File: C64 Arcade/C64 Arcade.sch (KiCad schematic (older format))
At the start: 59 parts, among them J1 Port_1, J10 P2_FIRE3, J11 P1_FIRE1, J12 P1_FIRE2, J13 P1_FIRE3, J14 EXT_PWR, J15 DIR_LEFT, J2 Port_2, J3 DIR_RIGHT, J4 UP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

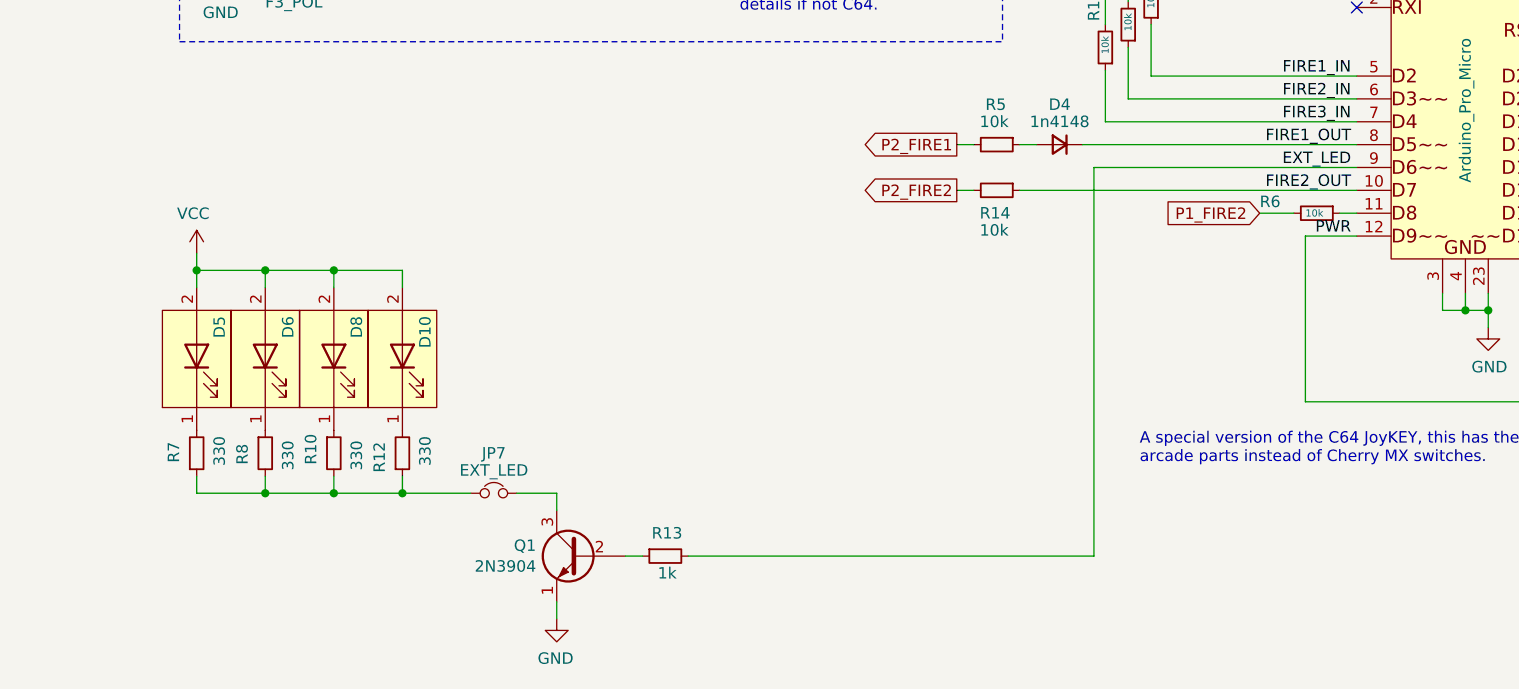
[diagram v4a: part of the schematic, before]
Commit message: New arcade layout
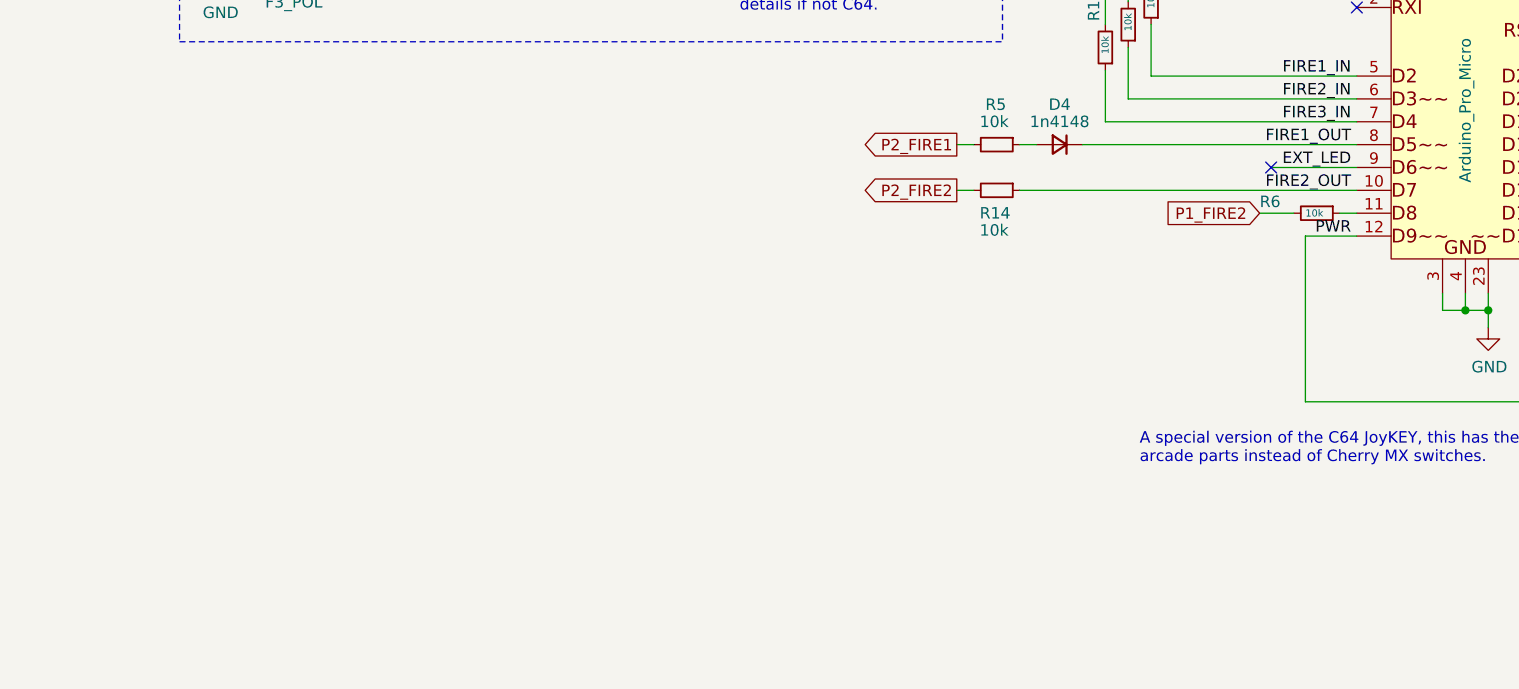
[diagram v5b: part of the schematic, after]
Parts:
- removed D10, D5, D6, D8: LED_Plugin, Connector_JST:JST_XH_B2B-XH-A_1x02_P2.50mm_Vertical, symbol arcade:LED_Plugin
- removed JP7: EXT_LED, Connector_PinHeader_2.54mm:PinHeader_1x02_P2.54mm_Horizontal, symbol Device:Jumper_NC_Small
- removed Q1: 2N3904, 2n3904:2N3904_TO-92_Horizontal_FlatSideDown, symbol Transistor_BJT:2N3904
- removed R10, R12, R7, R8: 330, Resistor_THT:R_Axial_DIN0207_L6.3mm_D2.5mm_P10.16mm_Horizontal, symbol Device:R_Small
- removed R13: 1k, Resistor_THT:R_Axial_DIN0207_L6.3mm_D2.5mm_P10.16mm_Horizontal, symbol Device:R_Small
- D3: footprint Diodes_THT:D_DO-41_SOD81_P10.16mm_Horizontal -> Diode_THT:D_DO-41_SOD81_P10.16mm_Horizontal
- J15: footprint (none) -> Connector_JST:JST_XH_B5B-XH-A_1x05_P2.50mm_Vertical
- JP1, JP2, JP3: footprint Pin_Headers:Pin_Header_Angled_1x03_Pitch2.54mm -> Connector_PinHeader_2.54mm:PinHeader_1x03_P2.54mm_Horizontal
- SW8: footprint Buttons_Switches_THT:SW_PUSH_6mm -> Button_Switch_THT:SW_PUSH_6mm
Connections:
- no-connect marks 8 -> 9
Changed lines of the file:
@@
 F 0 "JP3" H 4500 3625 50  0000 C CNN
 F 1 "FIRE3_SEL" H 4625 3700 50  0000 C CNN
-F 2 "Pin_Headers:Pin_Header_Angled_1x03_Pitch2.54mm" H 4400 3775 50  0001 C CNN
+F 2 "Connector_PinHeader_2.54mm:PinHeader_1x03_P2.54mm_Horizontal" H 4400 3775 50  0001 C CNN
 F 3 "~" H 4400 3775 50  0001 C CNN
 	1    4400 3775
@@
 F 0 "JP2" H 3325 4636 50  0000 C CNN
 F 1 "F3_POL" H 3325 4727 50  0000 C CNN
-F 2 "Pin_Headers:Pin_Header_Angled_1x03_Pitch2.54mm" H 3325 4525 50  0001 C CNN
+F 2 "Connector_PinHeader_2.54mm:PinHeader_1x03_P2.54mm_Horizontal" H 3325 4525 50  0001 C CNN
 F 3 "~" H 3325 4525 50  0001 C CNN
 	1    3325 4525
@@
 F 0 "D3" H 9975 1159 50  0000 C CNN
 F 1 "1n4001" H 9975 1250 50  0000 C CNN
-F 2 "Diodes_THT:D_DO-41_SOD81_P10.16mm_Horizontal" H 9975 1375 50  0001 C CNN
+F 2 "Diode_THT:D_DO-41_SOD81_P10.16mm_Horizontal" H 9975 1375 50  0001 C CNN
 F 3 "~" H 9975 1375 50  0001 C CNN
 	1    9975 1375
@@
 	1    0    0    -1
 $EndComp
-$Comp
-L Transistor_BJT:2N3904 Q1
-U 1 1 5FF9EE9A
-P 4575 7150
-F 0 "Q1" H 4765 7196 50  0000 L CNN
-F 1 "2N3904" H 4765 7105 50  0000 L CNN
-F 2 "2n3904:2N3904_TO-92_Horizontal_FlatSideDown" H 4775 7075 50  0001 L CIN
-F 3 "https://www.onsemi.com/pub/Collateral/2N3903-D.PDF" H 4575 7150 50  0001 L CNN
-	1    4575 7150
-	-1   0    0    -1
-$EndComp
-$Comp
-L power:GND #PWR0105
-U 1 1 60445FBA
-P 4475 7425
-F 0 "#PWR0105" H 4475 7175 50  0001 C CNN
-F 1 "GND" H 4480 7252 50  0000 C CNN
-F 2 "" H 4475 7425 50  0001 C CNN
-F 3 "" H 4475 7425 50  0001 C CNN
-	1    4475 7425
-	-1   0    0    -1
-$EndComp
-Wire Wire Line
-	4475 6950 4475 6875
-Wire Wire Line
-	3800 6800 3800 6875
-Wire Wire Line
-	3500 6800 3500 6875
-Wire Wire Line
-	3200 6800 3200 6875
-Wire Wire Line
-	3200 6875 2900 6875
-Wire Wire Line
-	2900 6800 2900 6875
-Wire Wire Line
-	3800 5975 3800 5900
-Wire Wire Line
-	3500 5900 3500 5975
-Wire Wire Line
-	3200 5900 3200 5975
-Wire Wire Line
-	3200 5900 2900 5900
-Wire Wire Line
-	2900 5900 2900 5975
-Connection ~ 2900 5900
-$Comp
-L power:VCC #PWR0106
-U 1 1 60445FBB
-P 2900 5825
-F 0 "#PWR0106" H 2900 5675 50  0001 C CNN
-F 1 "VCC" H 2915 5998 50  0000 C CNN
-F 2 "" H 2900 5825 50  0001 C CNN
-F 3 "" H 2900 5825 50  0001 C CNN
-	1    2900 5825
-	-1   0    0    -1
-$EndComp
-$Comp
-L Device:R_Small R13
-U 1 1 60445FBC
-P 4950 7150
-F 0 "R13" V 4850 7075 50  0000 L CNN
-F 1 "1k" V 5025 7100 50  0000 L CNN
-F 2 "Resistor_THT:R_Axial_DIN0207_L6.3mm_D2.5mm_P10.16mm_Horizontal" H 4950 7150 50  0001 C CNN
-F 3 "~" H 4950 7150 50  0001 C CNN
-	1    4950 7150
-	0    -1   1    0
-$EndComp
-Wire Wire Line
-	4850 7150 4775 7150
 Text GLabel 3400 2575 2    50   Output ~ 0
 FIRE2_POL
@@
 	3325 2575 3325 2675
 Wire Wire Line
-	6825 7150 6825 5450
-$Comp
-L Device:R_Small R7
-U 1 1 60445FBE
-P 2900 6700
-F 0 "R7" V 2800 6650 50  0000 L CNN
-F 1 "330" V 3000 6625 50  0000 L CNN
-F 2 "Resistor_THT:R_Axial_DIN0207_L6.3mm_D2.5mm_P10.16mm_Horizontal" H 2900 6700 50  0001 C CNN
-F 3 "~" H 2900 6700 50  0001 C CNN
-	1    2900 6700
-	1    0    0    1
-$EndComp
-$Comp
-L Device:R_Small R8
-U 1 1 60A50931
-P 3200 6700
-F 0 "R8" V 3100 6650 50  0000 L CNN
-F 1 "330" V 3300 6625 50  0000 L CNN
-F 2 "Resistor_THT:R_Axial_DIN0207_L6.3mm_D2.5mm_P10.16mm_Horizontal" H 3200 6700 50  0001 C CNN
-F 3 "~" H 3200 6700 50  0001 C CNN
-	1    3200 6700
-	1    0    0    -1
-$EndComp
-$Comp
-L Device:R_Small R10
-U 1 1 60152B72
-P 3500 6700
-F 0 "R10" V 3400 6650 50  0000 L CNN
-F 1 "330" V 3600 6625 50  0000 L CNN
-F 2 "Resistor_THT:R_Axial_DIN0207_L6.3mm_D2.5mm_P10.16mm_Horizontal" H 3500 6700 50  0001 C CNN
-F 3 "~" H 3500 6700 50  0001 C CNN
-	1    3500 6700
-	1    0    0    -1
-$EndComp
-$Comp
-L Device:R_Small R12
-U 1 1 60A50933
-P 3800 6700
-F 0 "R12" V 3700 6650 50  0000 L CNN
-F 1 "330" V 3900 6625 50  0000 L CNN
-F 2 "Resistor_THT:R_Axial_DIN0207_L6.3mm_D2.5mm_P10.16mm_Horizontal" H 3800 6700 50  0001 C CNN
-F 3 "~" H 3800 6700 50  0001 C CNN
-	1    3800 6700
-	1    0    0    1
-$EndComp
-Wire Wire Line
-	4475 7425 4475 7350
-Wire Wire Line
 	4400 3625 4400 3550
-$Comp
-L Device:Jumper_NC_Small JP7
-U 1 1 603A8E18
-P 4200 6875
-F 0 "JP7" H 4200 7050 50  0000 C CNN
-F 1 "EXT_LED" H 4200 6975 50  0000 C CNN
-F 2 "Connector_PinHeader_2.54mm:PinHeader_1x02_P2.54mm_Horizontal" H 4200 6875 50  0001 C CNN
-F 3 "~" H 4200 6875 50  0001 C CNN
-	1    4200 6875
-	-1   0    0    -1
-$EndComp
-Wire Wire Line
-	5050 7150 6825 7150
-Wire Wire Line
-	3800 6875 4100 6875
-Wire Wire Line
-	4300 6875 4475 6875
 Text Label 9050 5850 0    50   ~ 0
 SYS
@@
 F 0 "JP1" H 3325 3136 50  0000 C CNN
 F 1 "F2_POL" H 3325 3227 50  0000 C CNN
-F 2 "Pin_Headers:Pin_Header_Angled_1x03_Pitch2.54mm" H 3325 3025 50  0001 C CNN
+F 2 "Connector_PinHeader_2.54mm:PinHeader_1x03_P2.54mm_Horizontal" H 3325 3025 50  0001 C CNN
 F 3 "~" H 3325 3025 50  0001 C CNN
 	1    3325 3025
@@
 Connection ~ 4100 1075
 Connection ~ 4100 2250
-$Comp
-L arcade:LED_Plugin D10
-U 1 1 6013CF33
-P 3800 6275
-F 0 "D10" H 3975 6175 50  0000 R CNN
-F 1 "LED_Plugin" V 3743 6097 50  0001 R CNN
-F 2 "Connector_JST:JST_XH_B2B-XH-A_1x02_P2.50mm_Vertical" H 3800 6275 50  0001 C CNN
-F 3 "~" H 3800 6275 50  0001 C CNN
-	1    3800 6275
-	0    -1   -1   0
-$EndComp
-$Comp
-L arcade:LED_Plugin D8
-U 1 1 6018EAC5
-P 3500 6275
-F 0 "D8" H 3675 6175 50  0000 R CNN
-F 1 "LED_Plugin" V 3443 6097 50  0001 R CNN
-F 2 "Connector_JST:JST_XH_B2B-XH-A_1x02_P2.50mm_Vertical" H 3500 6275 50  0001 C CNN
-F 3 "~" H 3500 6275 50  0001 C CNN
-	1    3500 6275
-	0    -1   -1   0
-$EndComp
-$Comp
-L arcade:LED_Plugin D6
-U 1 1 601A1981
-P 3200 6275
-F 0 "D6" H 3375 6175 50  0000 R CNN
-F 1 "LED_Plugin" V 3143 6097 50  0001 R CNN
-F 2 "Connector_JST:JST_XH_B2B-XH-A_1x02_P2.50mm_Vertical" H 3200 6275 50  0001 C CNN
-F 3 "~" H 3200 6275 50  0001 C CNN
-	1    3200 6275
-	0    -1   -1   0
-$EndComp
-$Comp
-L arcade:LED_Plugin D5
-U 1 1 601AB1C0
-P 2900 6275
-F 0 "D5" H 3075 6175 50  0000 R CNN
-F 1 "LED_Plugin" V 2843 6097 50  0001 R CNN
-F 2 "Connector_JST:JST_XH_B2B-XH-A_1x02_P2.50mm_Vertical" H 2900 6275 50  0001 C CNN
-F 3 "~" H 2900 6275 50  0001 C CNN
-	1    2900 6275
-	0    -1   -1   0
-$EndComp
 $Comp
 L arcade:PWR J14
@@
 	1    0    0    -1
 $EndComp
-Wire Wire Line
-	2900 5825 2900 5900
 Text GLabel 7550 5650 0    50   Input ~ 0
 P1_FIRE2
@@
 	8850 1375 9550 1375
 Wire Wire Line
-	3200 6875 3500 6875
-Connection ~ 3200 6875
-Wire Wire Line
-	3500 6875 3800 6875
-Connection ~ 3500 6875
-Connection ~ 3800 6875
-Wire Wire Line
-	3200 5900 3500 5900
-Connection ~ 3200 5900
-Wire Wire Line
-	3500 5900 3800 5900
-Connection ~ 3500 5900
-Wire Wire Line
 	10200 1375 10275 1375
 Connection ~ 10200 1375
@@
 F 0 "J15" H 830 1025 50  0000 C CNN
 F 1 "DIR_LEFT" H 830 1116 50  0000 C CNN
-F 2 "" H 850 1450 50  0001 C CNN
+F 2 "Connector_JST:JST_XH_B5B-XH-A_1x05_P2.50mm_Vertical" H 850 1450 50  0001 C CNN
 F 3 "~" H 850 1450 50  0001 C CNN
 	1    850  1450
@@
 F 0 "SW8" H 9200 5025 50  0000 C CNN
 F 1 "RESET" H 9200 4775 50  0000 C CNN
-F 2 "Buttons_Switches_THT:SW_PUSH_6mm" H 9200 5050 50  0001 C CNN
+F 2 "Button_Switch_THT:SW_PUSH_6mm" H 9200 5050 50  0001 C CNN
 F 3 "~" H 9200 5050 50  0001 C CNN
 	1    9200 4850
@@
 Wire Wire Line
 	6875 4825 6875 3550
-Wire Wire Line
-	6825 5450 7975 5450
 Text Label 7950 5450 2    50   ~ 0
 EXT_LED
@@
 Wire Wire Line
 	3325 3875 3325 4175
+Wire Wire Line
+	7975 5450 7600 5450
+NoConn ~ 7600 5450
 $EndSCHEMATC

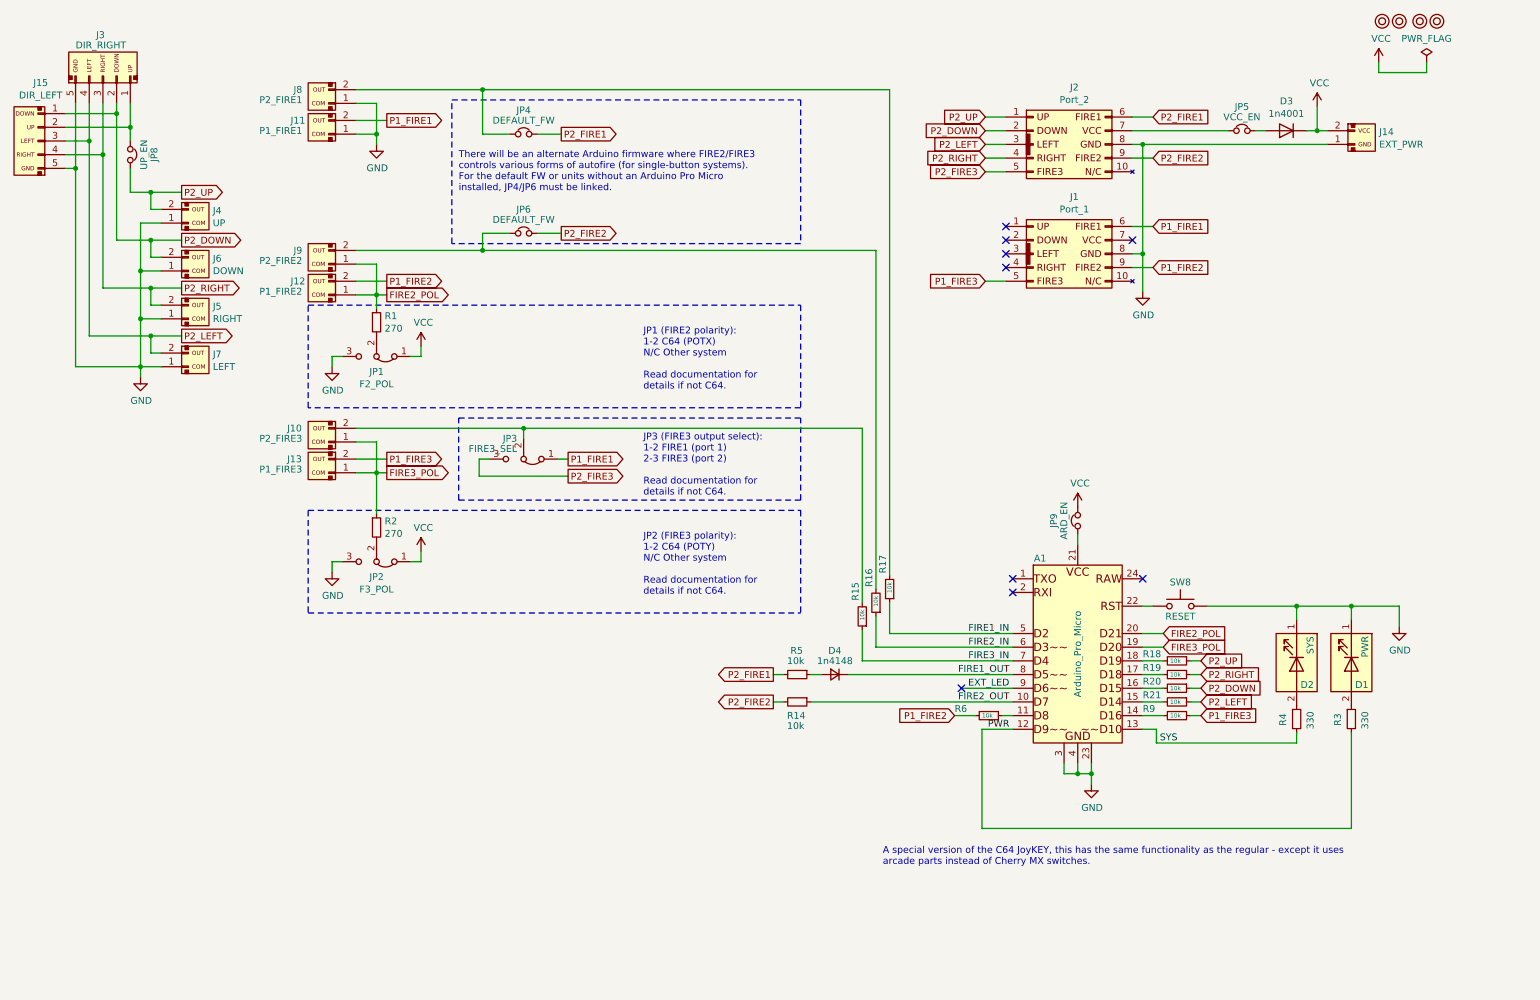
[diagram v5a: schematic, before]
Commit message: Add one more button to arcade board
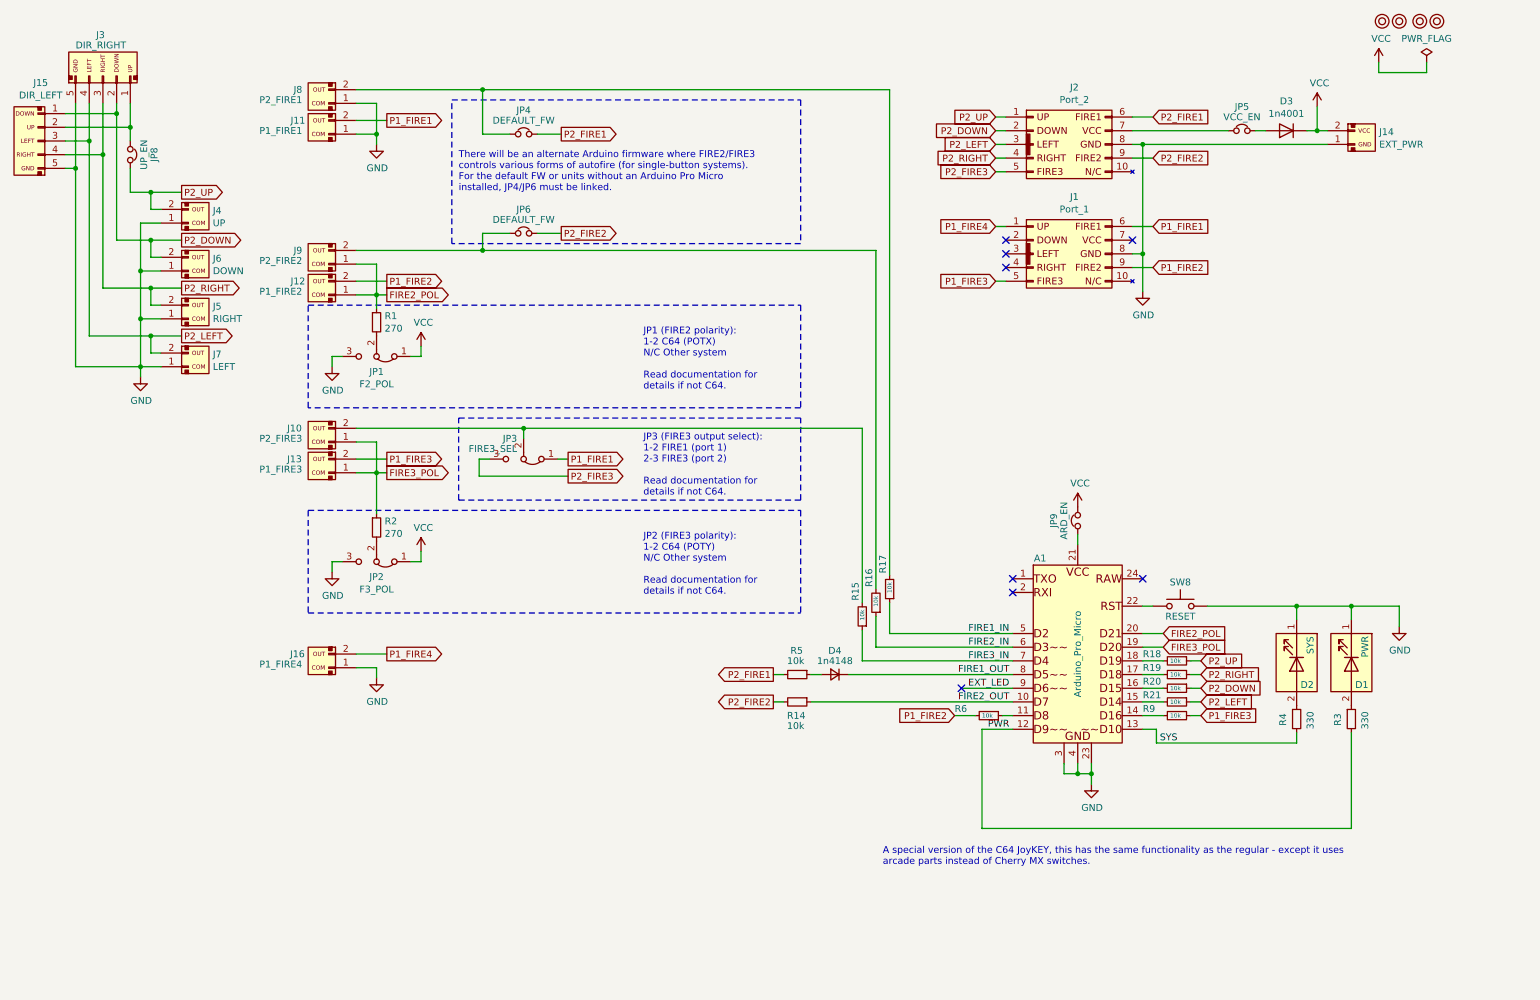
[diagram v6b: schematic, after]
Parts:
- added J16: P1_FIRE4, Connector_JST:JST_XH_B2B-XH-A_1x02_P2.50mm_Vertical, symbol arcade:SWITCH
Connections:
- net GND: now also J16.1 (Pin_1)
- net P1_FIRE4: now reaches J1.1 (Pin_1)
- net P1_FIRE4: now also J16.2 (Pin_2)
- no-connect marks 9 -> 8
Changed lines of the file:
@@
 	1    0    0    -1
 $EndComp
-NoConn ~ 7925 2075
 NoConn ~ 7925 2175
 NoConn ~ 7925 2275
 NoConn ~ 7925 2375
 NoConn ~ 8850 2175
-Text GLabel 7775 1275 0    50   Input ~ 0
+Text GLabel 7850 1275 0    50   Input ~ 0
 P2_UP
-Wire Wire Line
-	7775 1275 7925 1275
-Text GLabel 7775 1375 0    50   Input ~ 0
+Text GLabel 7850 1375 0    50   Input ~ 0
 P2_DOWN
-Wire Wire Line
-	7925 1375 7775 1375
-Text GLabel 7775 1475 0    50   Input ~ 0
+Text GLabel 7850 1475 0    50   Input ~ 0
 P2_LEFT
-Wire Wire Line
-	7775 1475 7925 1475
-Text GLabel 7775 1575 0    50   Input ~ 0
+Text GLabel 7850 1575 0    50   Input ~ 0
 P2_RIGHT
-Wire Wire Line
-	7775 1575 7925 1575
 Text GLabel 9000 1575 2    50   Input ~ 0
 P2_FIRE2
 Wire Wire Line
 	9000 1575 8850 1575
-Text GLabel 7775 1675 0    50   Input ~ 0
+Text GLabel 7850 1675 0    50   Input ~ 0
 P2_FIRE3
-Wire Wire Line
-	7775 1675 7925 1675
 $Comp
 L power:GND #PWR04
@@
 Wire Wire Line
 	9000 2375 8850 2375
-Text GLabel 7775 2475 0    50   Input ~ 0
+Text GLabel 7850 2475 0    50   Input ~ 0
 P1_FIRE3
-Wire Wire Line
-	7775 2475 7925 2475
 $Comp
 L arcade:SWITCH J4
@@
 	7975 5450 7600 5450
 NoConn ~ 7600 5450
+Text GLabel 7850 2075 0    50   Input ~ 0
+P1_FIRE4
+$Comp
+L power:GND #PWR09
+U 1 1 62E4482B
+P 3325 5375
+F 0 "#PWR09" H 3325 5125 50  0001 C CNN
+F 1 "GND" H 3330 5202 50  0000 C CNN
+F 2 "" H 3325 5375 50  0001 C CNN
+F 3 "" H 3325 5375 50  0001 C CNN
+	1    3325 5375
+	1    0    0    -1
+$EndComp
+$Comp
+L arcade:SWITCH J16
+U 1 1 62E44831
+P 2925 5250
+F 0 "J16" H 3050 5300 50  0000 L CNN
+F 1 "P1_FIRE4" H 3225 5225 50  0000 C CNN
+F 2 "Connector_JST:JST_XH_B2B-XH-A_1x02_P2.50mm_Vertical" H 2875 5400 50  0001 C CNN
+F 3 "~" H 2875 5400 50  0001 C CNN
+	1    2925 5250
+	-1   0    0    -1
+$EndComp
+Wire Wire Line
+	3175 5300 3325 5300
+Wire Wire Line
+	3325 5375 3325 5300
+Text GLabel 3400 5200 2    50   Output ~ 0
+P1_FIRE4
+Wire Wire Line
+	3175 5200 3400 5200
+Wire Wire Line
+	7925 1275 7850 1275
+Wire Wire Line
+	7925 1375 7850 1375
+Wire Wire Line
+	7925 1475 7850 1475
+Wire Wire Line
+	7925 1575 7850 1575
+Wire Wire Line
+	7925 1675 7850 1675
+Wire Wire Line
+	7925 2075 7850 2075
+Wire Wire Line
+	7850 2475 7925 2475
 $EndSCHEMATC
